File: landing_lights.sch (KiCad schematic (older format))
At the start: 24 parts, among them J21 JST-PA-3, J22 JST-PA-3, Q3 IRFZ44, Q4 IRFZ44, U10 74LS74, U11 74LS74, U12 MIC5014, U13 MIC5014

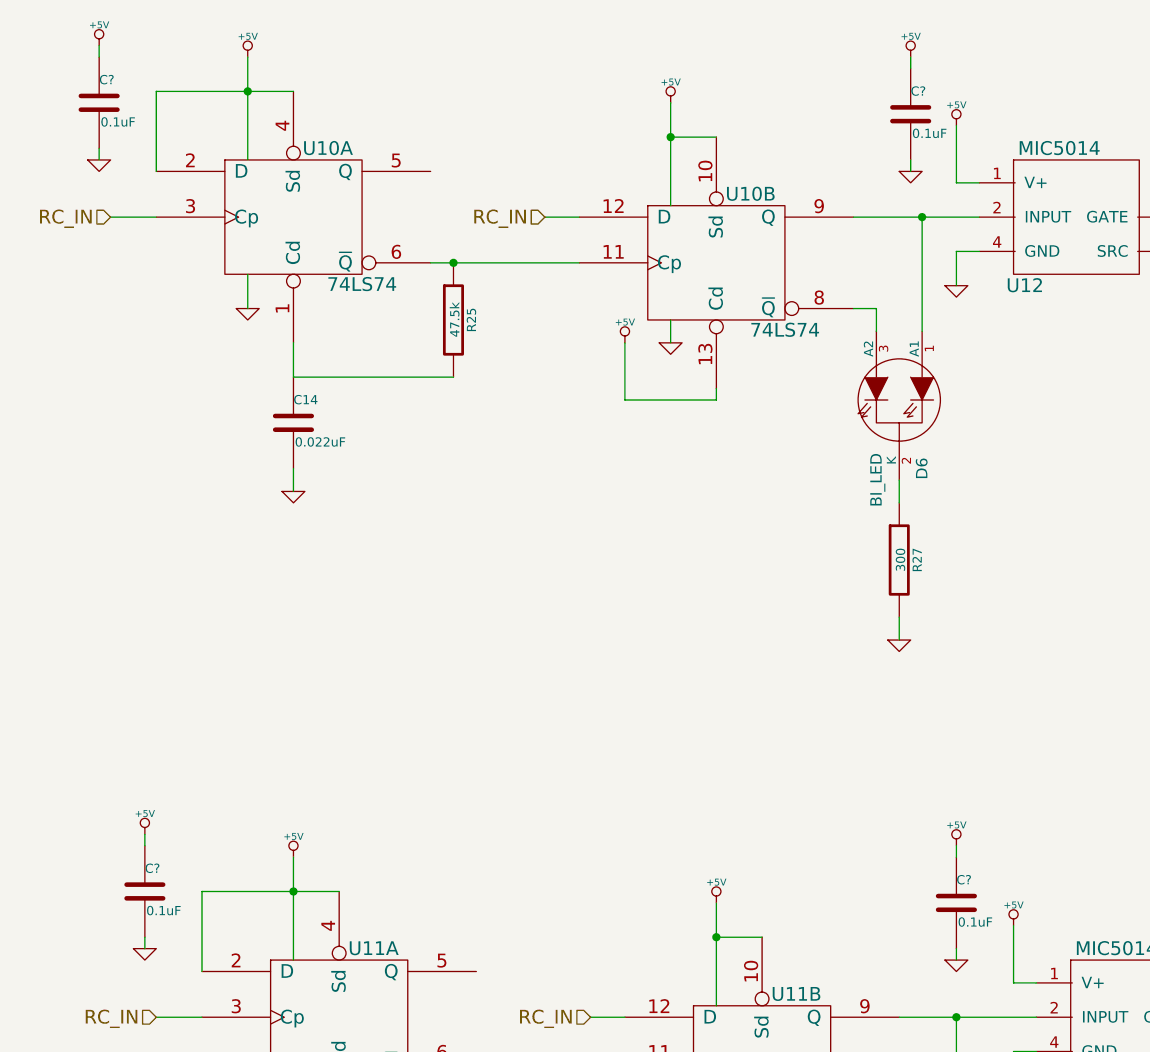
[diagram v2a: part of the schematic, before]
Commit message: Adding buffer on voltage reference output.
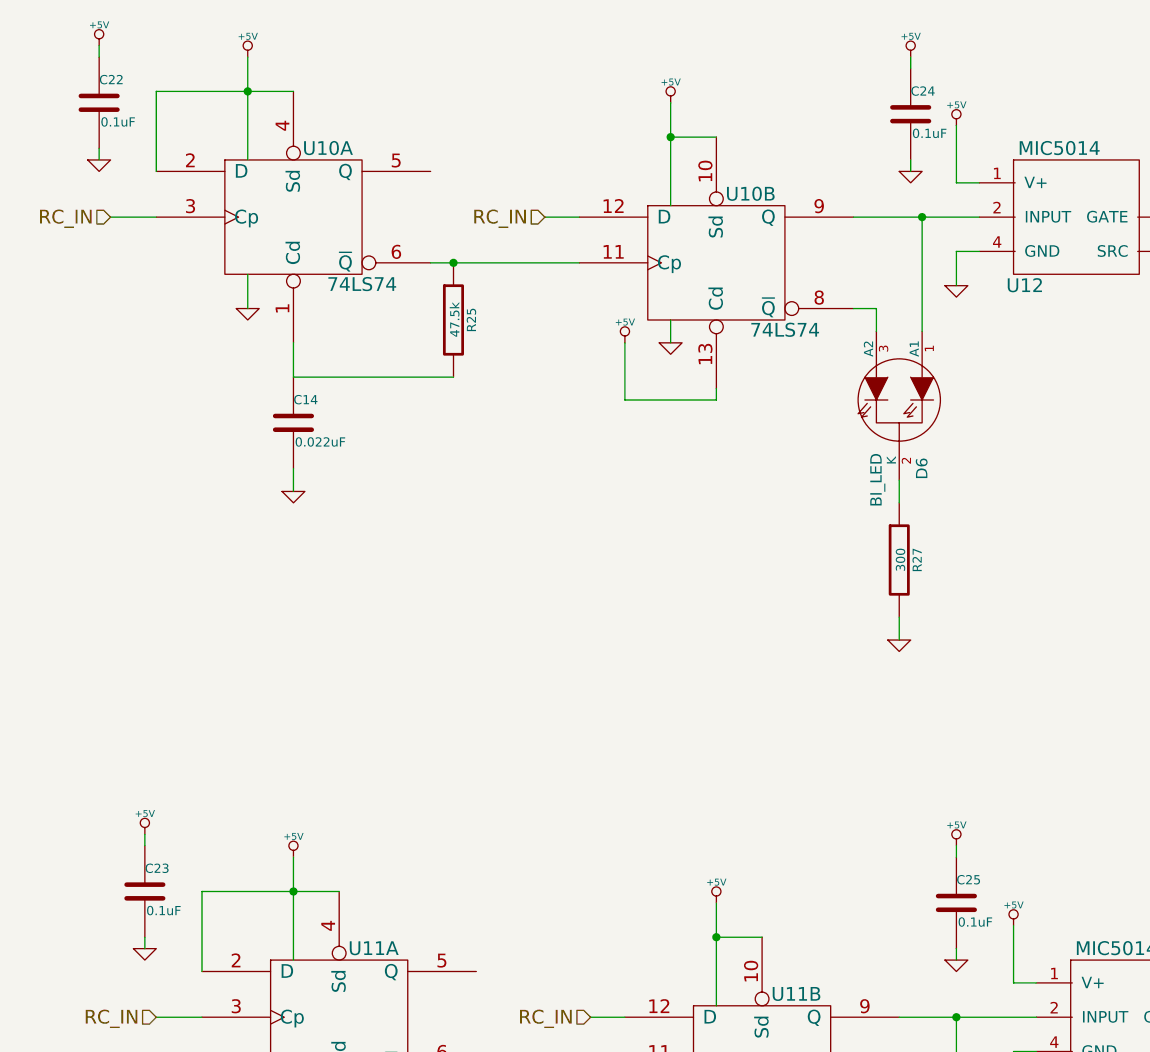
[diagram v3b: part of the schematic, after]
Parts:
- gave numbers to parts that had none: 4
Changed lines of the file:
@@
 $EndComp
 $Comp
-L +5V #PWR065
+L +5V #PWR079
 U 1 1 55D6B0A0
 P 3750 4650
-F 0 "#PWR065" H 3750 4740 20  0001 C CNN
+F 0 "#PWR079" H 3750 4740 20  0001 C CNN
 F 1 "+5V" H 3750 4740 30  0000 C CNN
 F 2 "" H 3750 4650 60  0000 C CNN
@@
 $EndComp
 $Comp
-L +5V #PWR066
+L +5V #PWR080
 U 1 1 55D6B0A2
 P 1900 4450
-F 0 "#PWR066" H 1900 4540 20  0001 C CNN
+F 0 "#PWR080" H 1900 4540 20  0001 C CNN
 F 1 "+5V" H 1900 4540 30  0000 C CNN
 F 2 "" H 1900 4450 60  0000 C CNN
@@
 $EndComp
 $Comp
-L GND #PWR067
+L GND #PWR081
 U 1 1 55D6B0A8
 P 2100 6350
-F 0 "#PWR067" H 2100 6350 30  0001 C CNN
+F 0 "#PWR081" H 2100 6350 30  0001 C CNN
 F 1 "GND" H 2100 6280 30  0001 C CNN
 F 2 "" H 2100 6350 60  0000 C CNN
@@
 	4550 5150 5150 5150
 $Comp
-L +5V #PWR068
+L +5V #PWR082
 U 1 1 55D6B0AA
 P 3550 5700
-F 0 "#PWR068" H 3550 5790 20  0001 C CNN
+F 0 "#PWR082" H 3550 5790 20  0001 C CNN
 F 1 "+5V" H 3550 5790 30  0000 C CNN
 F 2 "" H 3550 5700 60  0000 C CNN
@@
 $EndComp
 $Comp
-L +5V #PWR069
+L +5V #PWR083
 U 1 1 55D6B0AC
 P 5050 4750
-F 0 "#PWR069" H 5050 4840 20  0001 C CNN
+F 0 "#PWR083" H 5050 4840 20  0001 C CNN
 F 1 "+5V" H 5050 4840 30  0000 C CNN
 F 2 "" H 5050 4750 60  0000 C CNN
@@
 	5050 5000 5050 4750
 $Comp
-L GND #PWR070
+L GND #PWR084
 U 1 1 55D6B0AE
 P 1900 5550
-F 0 "#PWR070" H 1900 5550 30  0001 C CNN
+F 0 "#PWR084" H 1900 5550 30  0001 C CNN
 F 1 "GND" H 1900 5480 30  0001 C CNN
 F 2 "" H 1900 5550 60  0000 C CNN
@@
 	1900 5400 1900 5550
 $Comp
-L GND #PWR071
+L GND #PWR085
 U 1 1 55D6B0B0
 P 3750 5700
-F 0 "#PWR071" H 3750 5700 30  0001 C CNN
+F 0 "#PWR085" H 3750 5700 30  0001 C CNN
 F 1 "GND" H 3750 5630 30  0001 C CNN
 F 2 "" H 3750 5700 60  0000 C CNN
@@
 	3750 5600 3750 5700
 $Comp
-L GND #PWR072
+L GND #PWR086
 U 1 1 55D6B0B1
 P 5050 5450
-F 0 "#PWR072" H 5050 5450 30  0001 C CNN
+F 0 "#PWR086" H 5050 5450 30  0001 C CNN
 F 1 "GND" H 5050 5380 30  0001 C CNN
 F 2 "" H 5050 5450 60  0000 C CNN
@@
 $EndComp
 $Comp
-L +5V #PWR073
+L +5V #PWR087
 U 1 1 55CD3F3F
 P 3550 1150
-F 0 "#PWR073" H 3550 1240 20  0001 C CNN
+F 0 "#PWR087" H 3550 1240 20  0001 C CNN
 F 1 "+5V" H 3550 1240 30  0000 C CNN
 F 2 "" H 3550 1150 60  0000 C CNN
@@
 $EndComp
 $Comp
-L +5V #PWR074
+L +5V #PWR088
 U 1 1 55D6B0BB
 P 1700 950
-F 0 "#PWR074" H 1700 1040 20  0001 C CNN
+F 0 "#PWR088" H 1700 1040 20  0001 C CNN
 F 1 "+5V" H 1700 1040 30  0000 C CNN
 F 2 "" H 1700 950 60  0000 C CNN
@@
 $EndComp
 $Comp
-L GND #PWR075
+L GND #PWR089
 U 1 1 55D6B0C0
 P 1900 2850
-F 0 "#PWR075" H 1900 2850 30  0001 C CNN
+F 0 "#PWR089" H 1900 2850 30  0001 C CNN
 F 1 "GND" H 1900 2780 30  0001 C CNN
 F 2 "" H 1900 2850 60  0000 C CNN
@@
 	4350 1650 4900 1650
 $Comp
-L +5V #PWR076
+L +5V #PWR090
 U 1 1 55D6B0C3
 P 3350 2200
-F 0 "#PWR076" H 3350 2290 20  0001 C CNN
+F 0 "#PWR090" H 3350 2290 20  0001 C CNN
 F 1 "+5V" H 3350 2290 30  0000 C CNN
 F 2 "" H 3350 2200 60  0000 C CNN
@@
 $EndComp
 $Comp
-L +5V #PWR077
+L +5V #PWR091
 U 1 1 55D6B0C5
 P 4800 1250
-F 0 "#PWR077" H 4800 1340 20  0001 C CNN
+F 0 "#PWR091" H 4800 1340 20  0001 C CNN
 F 1 "+5V" H 4800 1340 30  0000 C CNN
 F 2 "" H 4800 1250 60  0000 C CNN
@@
 	4800 1500 4800 1250
 $Comp
-L GND #PWR078
+L GND #PWR092
 U 1 1 55D6B0C7
 P 1700 2050
-F 0 "#PWR078" H 1700 2050 30  0001 C CNN
+F 0 "#PWR092" H 1700 2050 30  0001 C CNN
 F 1 "GND" H 1700 1980 30  0001 C CNN
 F 2 "" H 1700 2050 60  0000 C CNN
@@
 	1700 1900 1700 2050
 $Comp
-L GND #PWR079
+L GND #PWR093
 U 1 1 55D6B0C8
 P 3550 2200
-F 0 "#PWR079" H 3550 2200 30  0001 C CNN
+F 0 "#PWR093" H 3550 2200 30  0001 C CNN
 F 1 "GND" H 3550 2130 30  0001 C CNN
 F 2 "" H 3550 2200 60  0000 C CNN
@@
 	3550 2100 3550 2200
 $Comp
-L GND #PWR080
+L GND #PWR094
 U 1 1 55D6B0CA
 P 4800 1950
-F 0 "#PWR080" H 4800 1950 30  0001 C CNN
+F 0 "#PWR094" H 4800 1950 30  0001 C CNN
 F 1 "GND" H 4800 1880 30  0001 C CNN
 F 2 "" H 4800 1950 60  0000 C CNN
@@
 RC_IN
 $Comp
-L +BATT #PWR081
+L +BATT #PWR095
 U 1 1 55CD3FB3
 P 6300 1300
-F 0 "#PWR081" H 6300 1250 20  0001 C CNN
+F 0 "#PWR095" H 6300 1250 20  0001 C CNN
 F 1 "+BATT" H 6300 1400 30  0000 C CNN
 F 2 "" H 6300 1300 60  0000 C CNN
@@
 $EndComp
 $Comp
-L +BATT #PWR082
+L +BATT #PWR096
 U 1 1 55CD3FCA
 P 6550 4800
-F 0 "#PWR082" H 6550 4750 20  0001 C CNN
+F 0 "#PWR096" H 6550 4750 20  0001 C CNN
 F 1 "+BATT" H 6550 4900 30  0000 C CNN
 F 2 "" H 6550 4800 60  0000 C CNN
@@
 $EndComp
 $Comp
-L GND #PWR083
+L GND #PWR097
 U 1 1 55D6B0D6
 P 4550 3500
-F 0 "#PWR083" H 4550 3500 30  0001 C CNN
+F 0 "#PWR097" H 4550 3500 30  0001 C CNN
 F 1 "GND" H 4550 3430 30  0001 C CNN
 F 2 "" H 4550 3500 60  0000 C CNN
@@
 $EndComp
 $Comp
-L GND #PWR084
+L GND #PWR098
 U 1 1 55D6B0DA
 P 4700 7000
-F 0 "#PWR084" H 4700 7000 30  0001 C CNN
+F 0 "#PWR098" H 4700 7000 30  0001 C CNN
 F 1 "GND" H 4700 6930 30  0001 C CNN
 F 2 "" H 4700 7000 60  0000 C CNN
@@
 $EndComp
 $Comp
-L GND #PWR085
+L GND #PWR099
 U 1 1 55D6B0DD
 P 9000 3600
-F 0 "#PWR085" H 9000 3600 30  0001 C CNN
+F 0 "#PWR099" H 9000 3600 30  0001 C CNN
 F 1 "GND" H 9000 3530 30  0001 C CNN
 F 2 "" H 9000 3600 60  0000 C CNN
@@
 	9100 4600 9000 4600
 $Comp
-L GND #PWR086
+L GND #PWR0100
 U 1 1 55CD6A29
 P 9000 4700
-F 0 "#PWR086" H 9000 4700 30  0001 C CNN
+F 0 "#PWR0100" H 9000 4700 30  0001 C CNN
 F 1 "GND" H 9000 4630 30  0001 C CNN
 F 2 "" H 9000 4700 60  0000 C CNN
@@
 $EndComp
 $Comp
-L C C?
+L C C22
 U 1 1 55D805D4
 P 1050 1150
-F 0 "C?" H 1050 1250 40  0000 L CNN
+F 0 "C22" H 1050 1250 40  0000 L CNN
 F 1 "0.1uF" H 1056 1065 40  0000 L CNN
 F 2 "SM0805" H 1088 1000 30  0001 C CNN
@@
 $EndComp
 $Comp
-L +5V #PWR?
+L +5V #PWR0101
 U 1 1 55D805DA
 P 1050 900
-F 0 "#PWR?" H 1050 990 20  0001 C CNN
+F 0 "#PWR0101" H 1050 990 20  0001 C CNN
 F 1 "+5V" H 1050 990 30  0000 C CNN
 F 2 "" H 1050 900 60  0000 C CNN
@@
 $EndComp
 $Comp
-L GND #PWR?
+L GND #PWR0102
 U 1 1 55D805E0
 P 1050 1400
-F 0 "#PWR?" H 1050 1400 30  0001 C CNN
+F 0 "#PWR0102" H 1050 1400 30  0001 C CNN
 F 1 "GND" H 1050 1330 30  0001 C CNN
 F 2 "" H 1050 1400 60  0000 C CNN
@@
 	1050 950  1050 900
 $Comp
-L C C?
+L C C24
 U 1 1 55D805E9
 P 4600 1200
-F 0 "C?" H 4600 1300 40  0000 L CNN
+F 0 "C24" H 4600 1300 40  0000 L CNN
 F 1 "0.1uF" H 4606 1115 40  0000 L CNN
 F 2 "SM0805" H 4638 1050 30  0001 C CNN
@@
 $EndComp
 $Comp
-L +5V #PWR?
+L +5V #PWR0103
 U 1 1 55D805EF
 P 4600 950
-F 0 "#PWR?" H 4600 1040 20  0001 C CNN
+F 0 "#PWR0103" H 4600 1040 20  0001 C CNN
 F 1 "+5V" H 4600 1040 30  0000 C CNN
 F 2 "" H 4600 950 60  0000 C CNN
@@
 $EndComp
 $Comp
-L GND #PWR?
+L GND #PWR0104
 U 1 1 55D805F5
 P 4600 1450
-F 0 "#PWR?" H 4600 1450 30  0001 C CNN
+F 0 "#PWR0104" H 4600 1450 30  0001 C CNN
 F 1 "GND" H 4600 1380 30  0001 C CNN
 F 2 "" H 4600 1450 60  0000 C CNN
@@
 	4600 1000 4600 950
 $Comp
-L C C?
+L C C23
 U 1 1 55D80613
 P 1250 4600
-F 0 "C?" H 1250 4700 40  0000 L CNN
+F 0 "C23" H 1250 4700 40  0000 L CNN
 F 1 "0.1uF" H 1256 4515 40  0000 L CNN
 F 2 "SM0805" H 1288 4450 30  0001 C CNN
@@
 $EndComp
 $Comp
-L +5V #PWR?
+L +5V #PWR0105
 U 1 1 55D80619
 P 1250 4350
-F 0 "#PWR?" H 1250 4440 20  0001 C CNN
+F 0 "#PWR0105" H 1250 4440 20  0001 C CNN
 F 1 "+5V" H 1250 4440 30  0000 C CNN
 F 2 "" H 1250 4350 60  0000 C CNN
@@
 $EndComp
 $Comp
-L GND #PWR?
+L GND #PWR0106
 U 1 1 55D8061F
 P 1250 4850
-F 0 "#PWR?" H 1250 4850 30  0001 C CNN
+F 0 "#PWR0106" H 1250 4850 30  0001 C CNN
 F 1 "GND" H 1250 4780 30  0001 C CNN
 F 2 "" H 1250 4850 60  0000 C CNN
@@
 	1250 4400 1250 4350
 $Comp
-L C C?
+L C C25
 U 1 1 55D8081D
 P 4800 4650
-F 0 "C?" H 4800 4750 40  0000 L CNN
+F 0 "C25" H 4800 4750 40  0000 L CNN
 F 1 "0.1uF" H 4806 4565 40  0000 L CNN
 F 2 "SM0805" H 4838 4500 30  0001 C CNN
@@
 $EndComp
 $Comp
-L +5V #PWR?
+L +5V #PWR0107
 U 1 1 55D80823
 P 4800 4400
-F 0 "#PWR?" H 4800 4490 20  0001 C CNN
+F 0 "#PWR0107" H 4800 4490 20  0001 C CNN
 F 1 "+5V" H 4800 4490 30  0000 C CNN
 F 2 "" H 4800 4400 60  0000 C CNN
@@
 $EndComp
 $Comp
-L GND #PWR?
+L GND #PWR0108
 U 1 1 55D80829
 P 4800 4900
-F 0 "#PWR?" H 4800 4900 30  0001 C CNN
+F 0 "#PWR0108" H 4800 4900 30  0001 C CNN
 F 1 "GND" H 4800 4830 30  0001 C CNN
 F 2 "" H 4800 4900 60  0000 C CNN
